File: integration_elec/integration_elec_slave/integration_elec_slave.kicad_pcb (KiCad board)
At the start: 4 copper layers, 102 parts, among them J1 CONN_02X05, J2 USB_C_Receptacle_USB2.0_16P, J3 Conn_01x03_Pin, J4 Conn_01x04_Pin, J5 Conn_01x04_Pin, Q1 Q_NMOS_GSD, Q2 Q_NMOS_GSD, Q3 Q_NMOS_GSD, SW1 SW_Push, U1 XBEE_PRO_900HP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

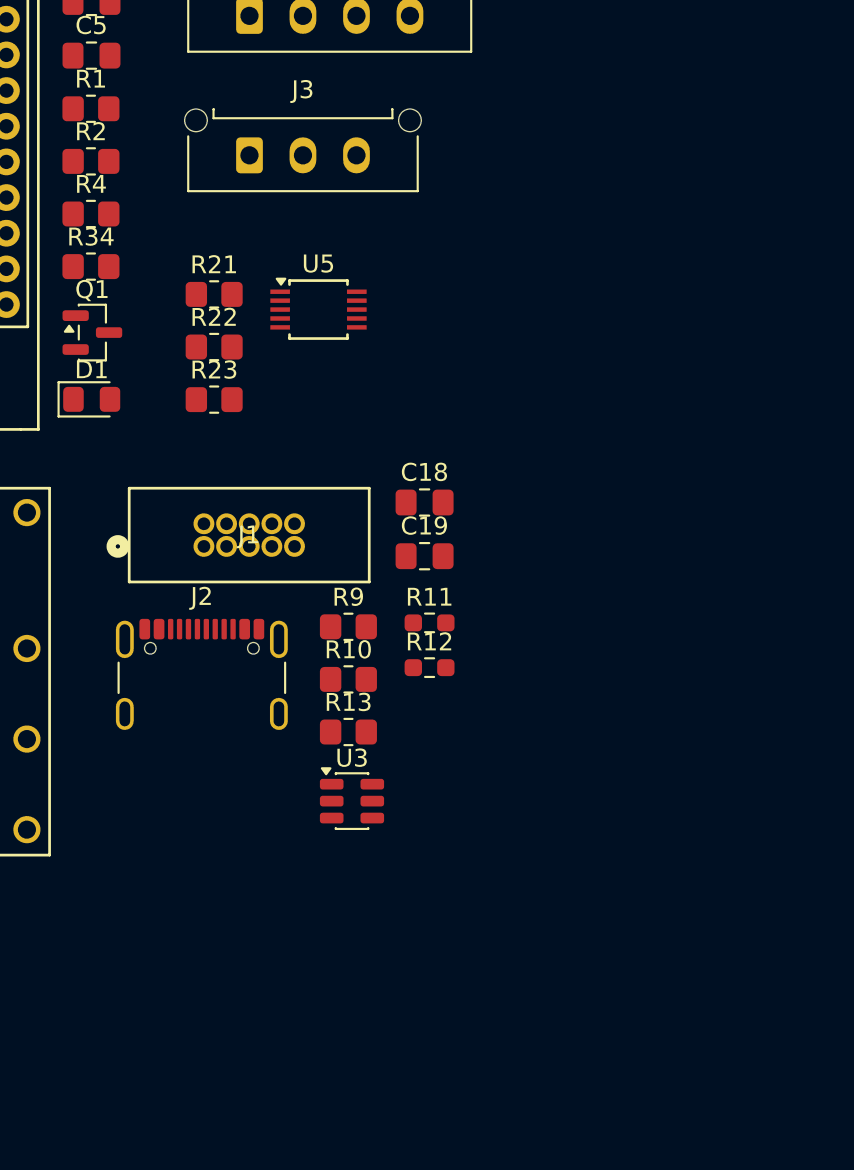
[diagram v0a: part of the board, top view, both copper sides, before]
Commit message: EM - Ajout John Pork et debut schematic
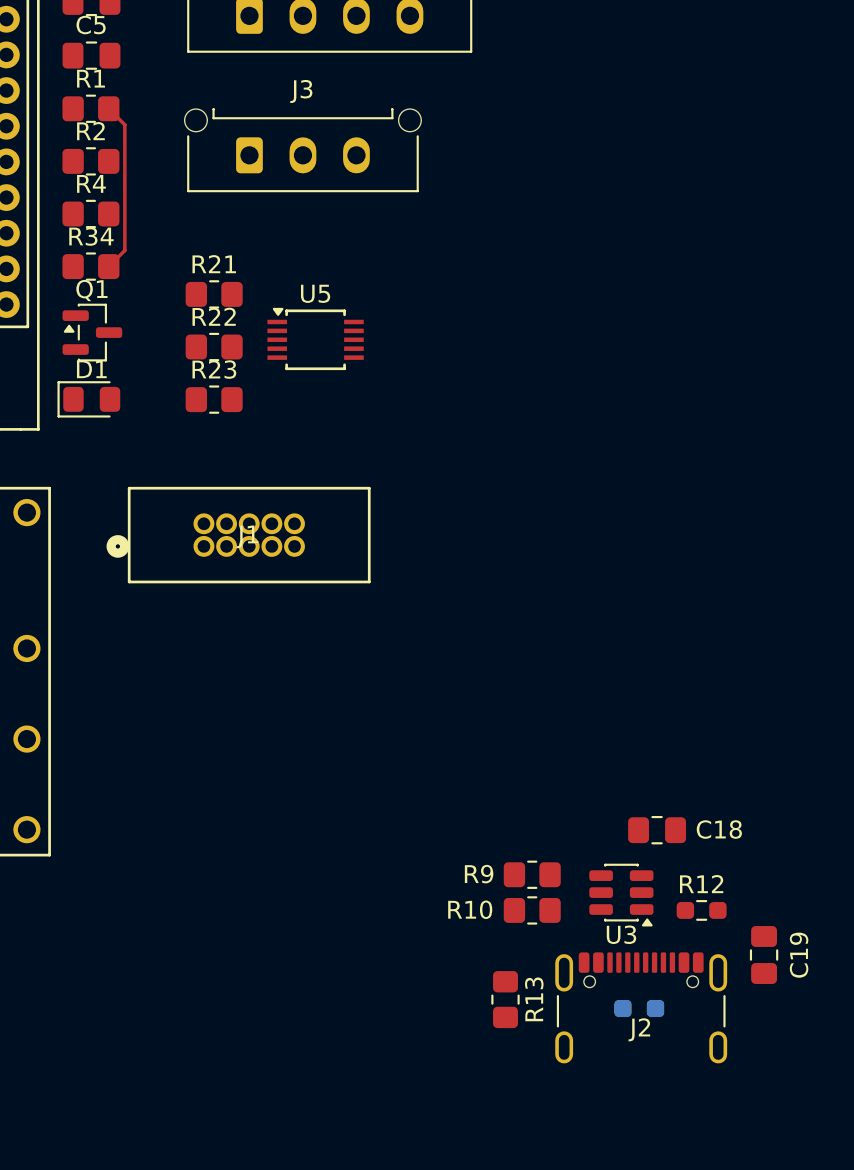
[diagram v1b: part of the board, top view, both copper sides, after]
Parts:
- R11: moved to B.Cu
- moved J2 30.9 mm to (235.1, 116.1)
- moved C19 29.4 mm to (242.0, 112.0), turned to 90 degrees
- moved R11 24.6 mm to (235.0, 115.0)
- moved C18 22.5 mm to (236.0, 105.0), turned to 180 degrees
- moved R12 20.4 mm to (238.5, 109.5)
- moved R13 17.4 mm to (227.5, 114.5), turned to -90 degrees
- moved R9 17.3 mm to (229.0, 107.5), turned to 180 degrees
- moved R10 16.6 mm to (229.0, 109.5), turned to 180 degrees
- moved U3 16.0 mm to (234.0, 108.5), turned to 180 degrees
- moved U5 1.70 mm to (216.8, 77.5)
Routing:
- net Net-(U1-nDTR): track 0.00 -> 9.60 mm
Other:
- copper layers 4 -> 2

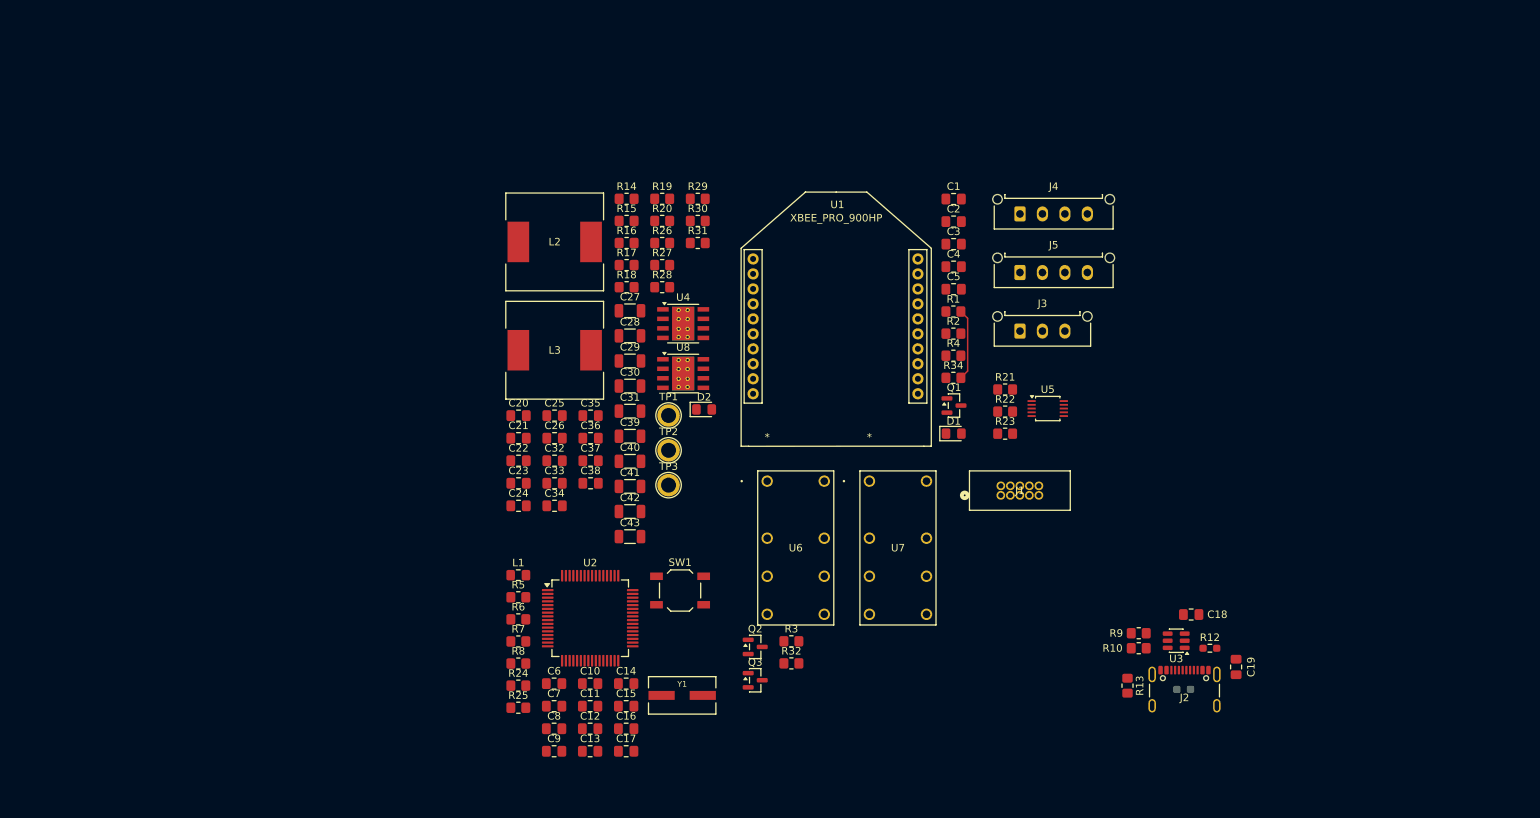
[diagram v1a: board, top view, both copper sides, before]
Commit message: EM - Fin du schématique, ajout de diode pour empêcher de backfeeder le USB. Début PCB et ajout carré 100x100
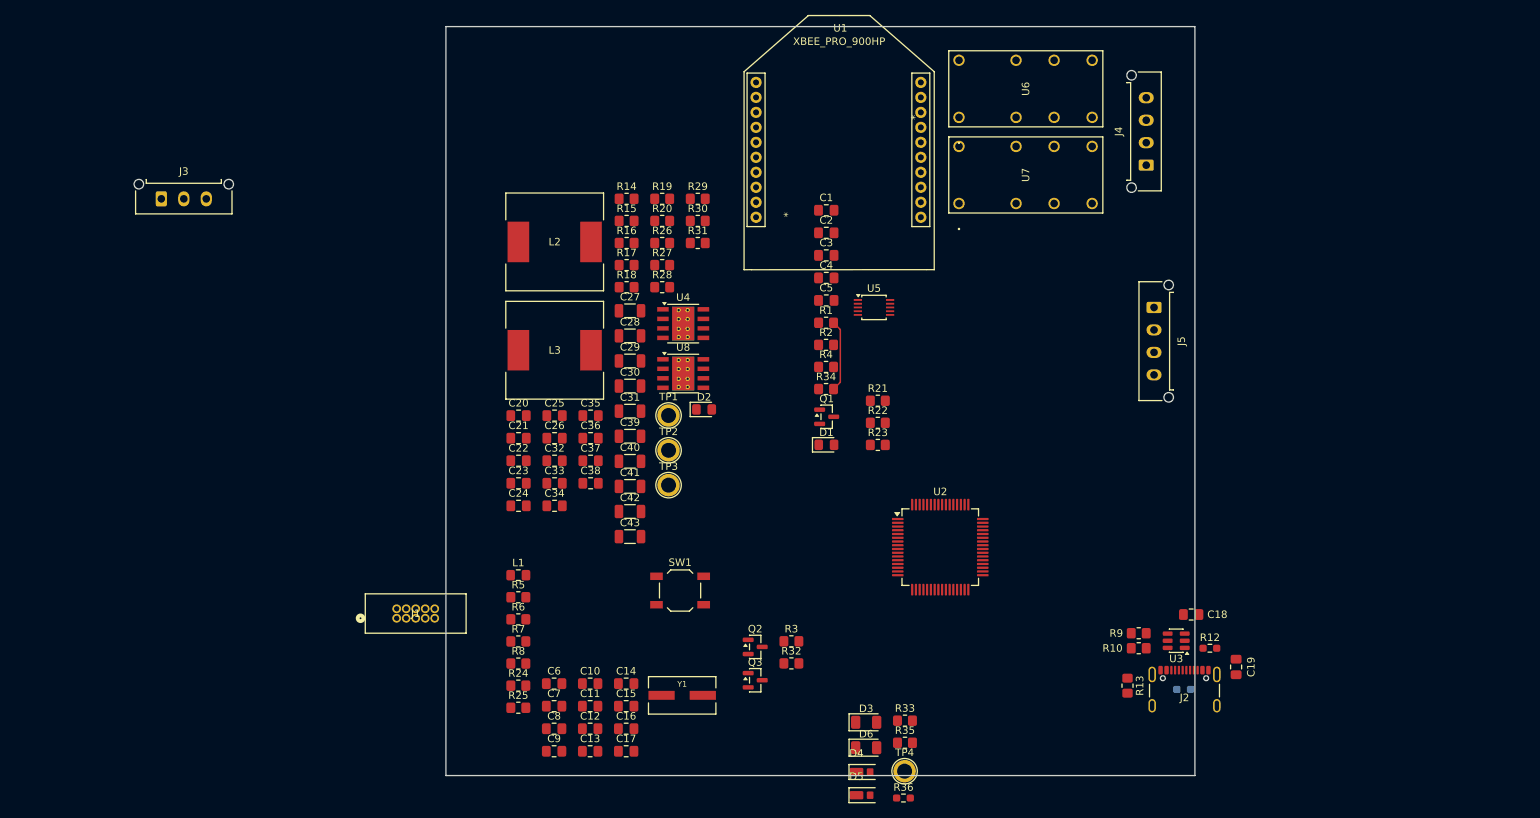
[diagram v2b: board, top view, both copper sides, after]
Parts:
- added D3: YELLOW LED, LED_SMD:LED_1206_3216Metric, F.Cu at (192.6, 119.4)
- added D4: D_Schottky, SCHTKY_DIODE:SOD323-HE, F.Cu at (191.3, 126.0)
- added D5: D_Schottky, SCHTKY_DIODE:SOD323-HE, F.Cu at (191.3, 129.1)
- added D6: GREEN LED, LED_SMD:LED_1206_3216Metric, F.Cu at (192.6, 122.8)
- added R33: 475, Resistor_SMD:R_0805_2012Metric_Pad1.20x1.40mm_HandSolder, F.Cu at (197.8, 119.2)
- added R35: 165, Resistor_SMD:R_0805_2012Metric_Pad1.20x1.40mm_HandSolder, F.Cu at (197.8, 122.1)
- added R36: 10k0, Resistor_SMD:R_0603_1608Metric_Pad0.98x0.95mm_HandSolder, F.Cu at (197.6, 129.5)
- added TP4: 12V+, TestPoint:TestPoint_Plated_Hole_D2.0mm, F.Cu at (197.7, 125.9)
- moved J3 116.0 mm to (98.5, 49.5)
- moved J1 82.3 mm to (129.9, 105.5)
- moved U6 54.9 mm to (205.0, 38.6), turned to 90 degrees
- moved U2 47.7 mm to (202.5, 96.0)
- moved U7 39.0 mm to (205.0, 50.1), turned to 90 degrees
- moved U5 26.8 mm to (193.7, 64.0)
- moved U1 23.6 mm to (177.9, 34.0)
- moved J5 18.5 mm to (231.0, 64.0), turned to -90 degrees
- moved J4 18.1 mm to (230.0, 45.0), turned to 90 degrees
- moved C1 17.1 mm to (187.3, 51.0)
- moved C2 17.1 mm to (187.3, 54.0)
- moved C3 17.1 mm to (187.3, 57.0)
- moved C4 17.1 mm to (187.3, 60.1)
- moved C5 17.1 mm to (187.3, 63.1)
- moved D1 17.1 mm to (187.3, 82.3)
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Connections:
- C20 pad 2: +12V -> /Regulator/REG_IN
- C21 pad 2: +12V -> /Regulator/REG_IN
- C22 pad 2: +12V -> /Regulator/REG_IN
- C23 pad 1: +12V -> /Regulator/REG_IN
- C32 pad 2: +12V -> /Regulator/REG_IN
- C33 pad 2: +12V -> /Regulator/REG_IN
- C34 pad 2: +12V -> /Regulator/REG_IN
- C35 pad 1: +12V -> /Regulator/REG_IN
- R14 pad 1: +12V -> /Regulator/REG_IN
- R26 pad 1: +12V -> /Regulator/REG_IN
- U4 pad 2: +12V -> /Regulator/REG_IN
- U8 pad 2: +12V -> /Regulator/REG_IN
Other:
- board outline added: 100 x 100 mm

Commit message: EM - Avancement du placement du PCB, fini USB et RELAIS, en train de continuer micro et regulateurs
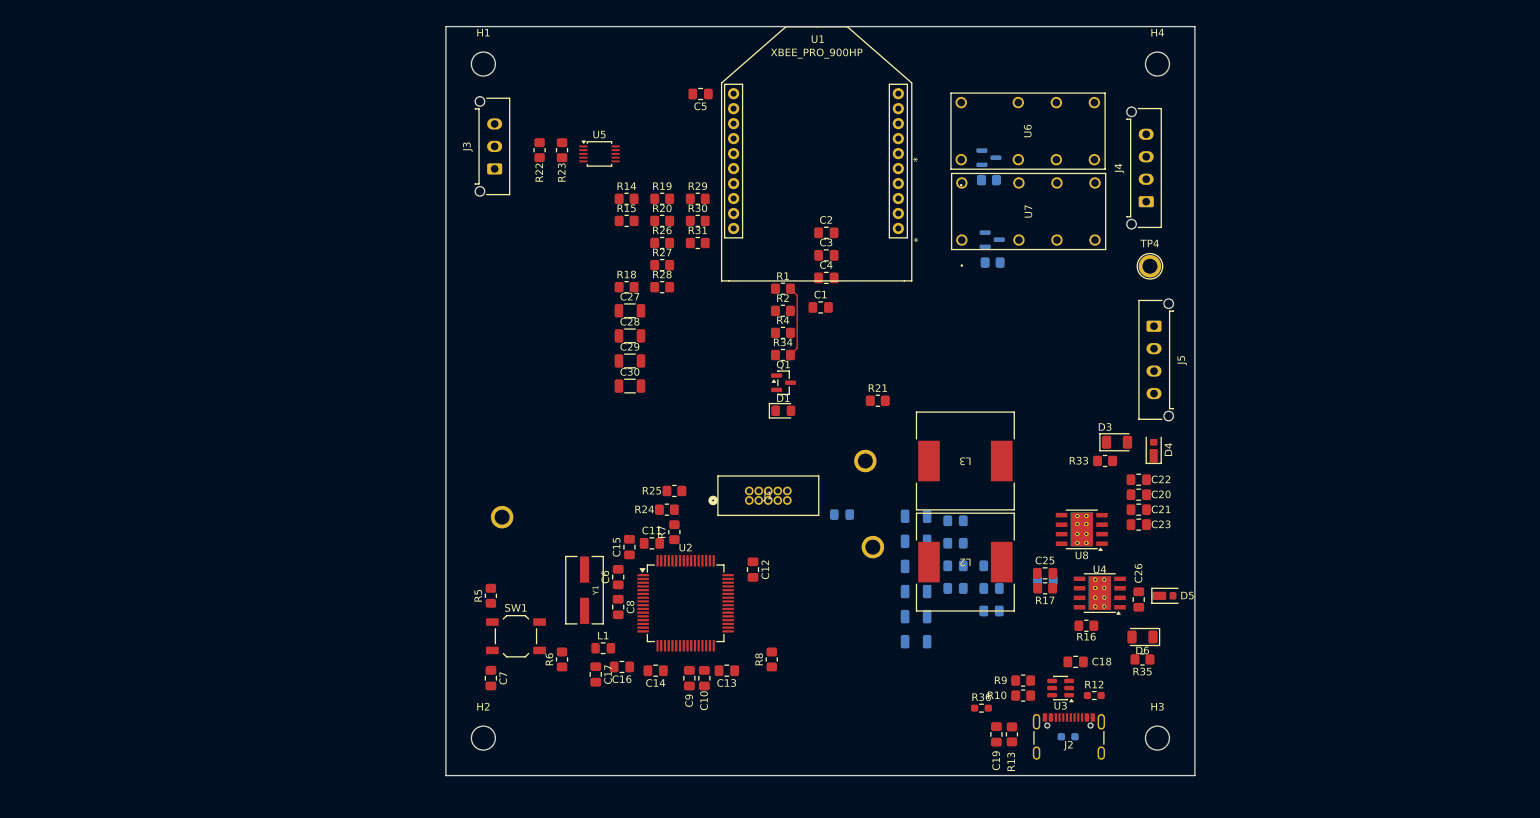
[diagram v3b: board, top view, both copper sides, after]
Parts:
- added H1: MountingHole, MountingHole:MountingHole_3.2mm_M3, F.Cu at (141.5, 31.5)
- added H2: MountingHole, MountingHole:MountingHole_3.2mm_M3, F.Cu at (141.5, 121.5)
- added H3: MountingHole, MountingHole:MountingHole_3.2mm_M3, F.Cu at (231.5, 121.5)
- added H4: MountingHole, MountingHole:MountingHole_3.2mm_M3, F.Cu at (231.5, 31.5)
- C24, C31, C32, C33, C34, C35, C36, C37, C38, C39, C40, C41, C42, C43, D2, Q2, Q3, R3, R32, TP1, TP2, TP3: moved to B.Cu
- U6, U7: footprint RELAY:RELAY8_J104D2C12VDC.20S_CRS -> RELAYS:RELAY8_J104D2C12VDC.20S_CRS
- moved C20 83.5 mm to (229.0, 89.0)
- moved C21 83.4 mm to (229.0, 91.0)
- moved C23 83.0 mm to (229.0, 93.0), turned to 180 degrees
- moved C22 82.8 mm to (229.0, 87.0)
- moved C26 80.9 mm to (229.0, 103.0), turned to 90 degrees
- moved R16 79.9 mm to (222.0, 106.5)
- moved TP4 75.0 mm to (230.5, 58.5)
- moved Q2 72.4 mm to (209.0, 44.0)
- moved C24 71.1 mm to (216.5, 100.5), turned to 180 degrees
- moved R17 70.6 mm to (216.5, 101.5), turned to 180 degrees
- moved L2 69.5 mm to (205.9, 98.0), turned to 180 degrees
- moved C25 68.8 mm to (216.5, 99.5)
- moved R3 67.0 mm to (209.0, 47.0)
- moved Q3 66.8 mm to (209.4, 55.0)
- moved U4 66.2 mm to (223.8, 102.1), turned to 180 degrees
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
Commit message: EM - Ajout du copper zone et chaise musicale pour le micro et le USB
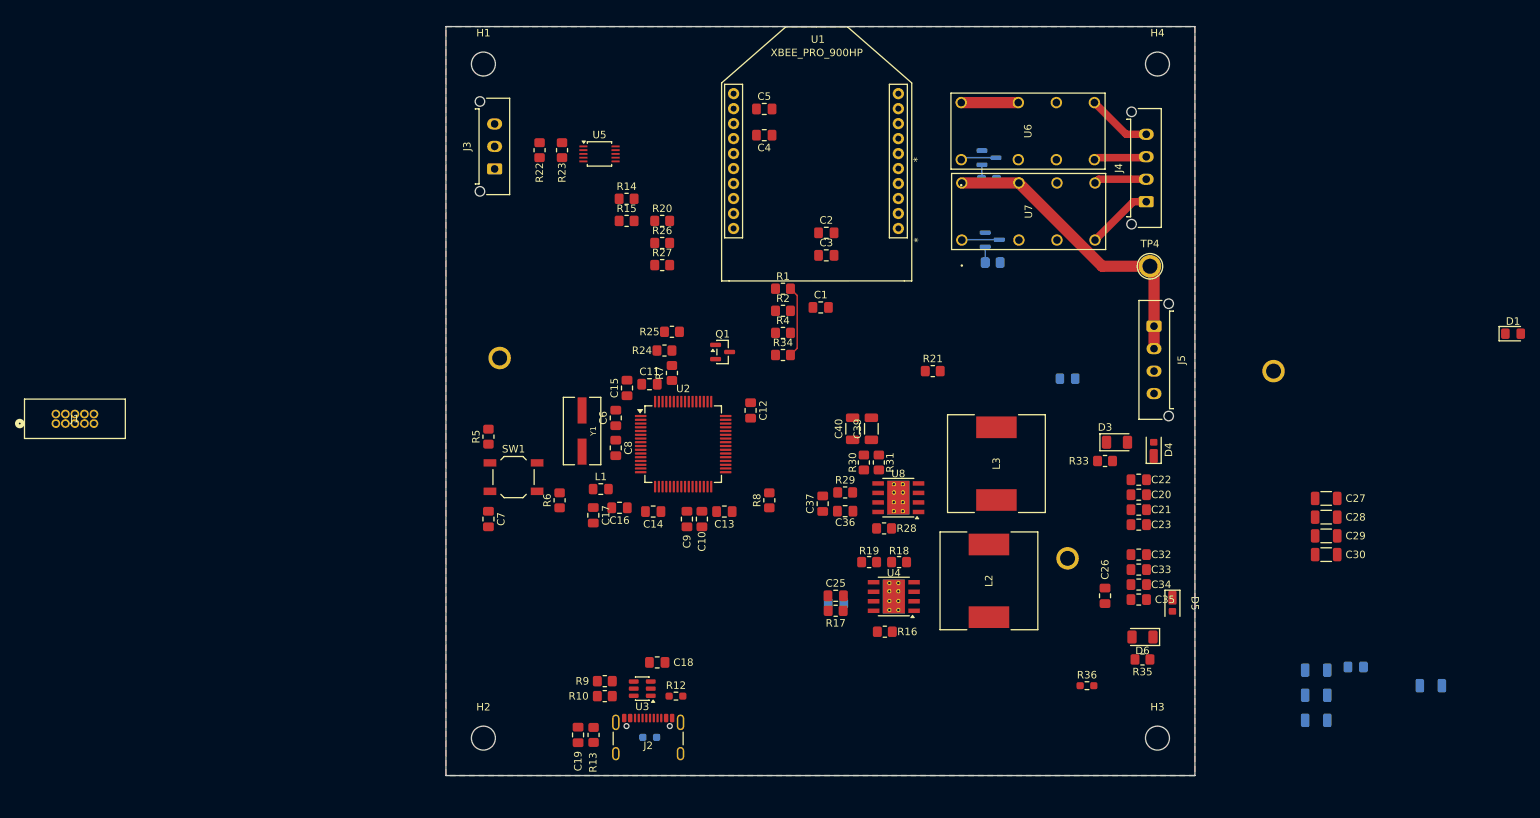
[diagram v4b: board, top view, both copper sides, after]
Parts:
- C32, C33, C34, C35, C36, C37, C39, C40: moved to F.Cu
- moved D1 98.0 mm to (279.0, 67.5)
- moved C27 96.3 mm to (254.0, 89.5)
- moved C28 96.1 mm to (254.0, 92.0)
- moved C29 95.8 mm to (254.0, 94.5)
- moved C30 95.6 mm to (254.0, 97.0)
- moved J1 93.1 mm to (84.4, 79.5)
- moved C31 72.3 mm to (268.0, 114.5)
- moved J2 56.2 mm to (163.5, 122.5)
- moved C19 55.9 mm to (154.1, 121.1)
- moved C18 55.9 mm to (164.7, 111.4)
- moved R10 55.9 mm to (157.7, 115.9)
- moved R11 55.9 mm to (163.7, 121.4)
- moved R12 55.9 mm to (167.2, 115.9)
- moved R13 55.9 mm to (156.2, 121.1)
- moved R9 55.9 mm to (157.7, 113.9)
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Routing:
- net +12V: track 0.00 -> 48.6 mm
- net /CONNECTORS/SOLENOID2_-: track 0.00 -> 8.96 mm
- net /CONNECTORS/SOLENOID1_+: track 0.00 -> 8.67 mm
- net /CONNECTORS/SOLENOID1_-: track 0.00 -> 7.08 mm
- net /CONNECTORS/SOLENOID2_+: track 0.00 -> 7.05 mm
- net Net-(Q3-D): track 0.00 -> 5.02 mm
- net Net-(Q2-D): track 0.00 -> 4.75 mm
- net /GESTION_ALIM/CTRL_SOL2: track 0.00 -> 2.10 mm
- net /GESTION_ALIM/CTRL_SOL1: track 0.00 -> 2.08 mm
- added copper zone on B.Cu, net GND
- added copper zone on F.Cu, net GND

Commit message: EM - PCB pas mal terminé, on review ça soon
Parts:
- C24, C31, C41, C42, C43, D2, TP3: moved to F.Cu
- C26: moved to B.Cu
- moved J1 96.7 mm to (181.0, 84.5), turned to -90 degrees
- moved D1 81.2 mm to (198.0, 62.0)
- moved R14 73.6 mm to (202.5, 110.0), turned to 180 degrees
- moved C31 70.7 mm to (200.5, 93.5), turned to 90 degrees
- moved R15 68.9 mm to (198.5, 110.0), turned to 180 degrees
- moved C43 67.6 mm to (201.5, 75.0), turned to 90 degrees
- moved C41 67.5 mm to (196.5, 75.0), turned to 90 degrees
- moved C42 67.4 mm to (199.0, 75.0), turned to 90 degrees
- moved C27 63.7 mm to (190.5, 93.5), turned to 90 degrees
- moved C28 61.0 mm to (193.0, 93.5), turned to 90 degrees
- moved C38 60.1 mm to (204.0, 85.5), turned to 90 degrees
- moved C29 58.5 mm to (195.5, 93.5), turned to 90 degrees
- moved C30 56.1 mm to (198.0, 93.5), turned to 90 degrees
- moved R35 52.1 mm to (178.0, 119.0), turned to -90 degrees
- moved D5 52.0 mm to (183.0, 115.0), turned to 90 degrees
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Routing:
- net +3V3: track 0.00 -> 284.7 mm, vias 0 -> 4
- net /Regulator/REG_IN: track 0.00 -> 129.7 mm
- net +5V: track 0.00 -> 90.4 mm, vias 0 -> 1
- net /MCU/RF.XBEE_LED: track 0.00 -> 61.1 mm, vias 0 -> 6
- net /GESTION_ALIM/CTRL_SOL1: track 2.08 -> 61.0 mm, vias 0 -> 1
- net /MCU/DEBUG_RESET: track 0.00 -> 57.2 mm, vias 0 -> 1
- net /GESTION_ALIM/CTRL_SOL2: track 2.10 -> 55.5 mm, vias 0 -> 1
- net /MCU/RF.XBEE_UART_OUT: track 0.00 -> 50.4 mm, vias 0 -> 1
- net /MCU/RF.XBEE_STATUS: track 0.00 -> 49.0 mm, vias 0 -> 1
- net /MCU/RF.XBEE_UART_IN: track 0.00 -> 48.0 mm, vias 0 -> 4
- net /MCU/RF.XBEE_UART_RTS: track 0.00 -> 47.7 mm, vias 0 -> 3
- net /ADC/INT_ADC_OD: track 0.00 -> 46.0 mm, vias 0 -> 2
- net /MCU/RF.XBEE_UART_CTS: track 0.00 -> 43.1 mm, vias 0 -> 1
- net /MCU/USB_D-: track 0.00 -> 41.0 mm
- net /MCU/USB_VBUS: track 0.00 -> 40.0 mm
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
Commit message: EM - Attente de review, complété avec les 3D
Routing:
- net GND: vias 8 -> 64

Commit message: EM - Oublié de run le script de via-stitching
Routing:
- net GND: vias 64 -> 905

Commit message: EM - Review pas mal finale
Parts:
- added G***: LOGO, LOGO, F.Cu at (147.0, 103.0)
- added G***: LOGO, LOGO, B.Cu at (159.3, 93.4)
- added G***: LOGO, LOGO, B.Cu at (206.9, 73.9)
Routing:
- net GND: track 25.5 -> 32.1 mm, vias 905 -> 878
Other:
- board text added: "12V"
- board text added: "3.3"
- board text added: "5V"
- board text added: "GND"
- board text added: "JTAG DEBUG"
- board text added: "POWER_IN_12V"
- board text added: "PRESSURE METER"
- board text added: "RESET SWITCH"
- board text added: "SOLENOIDS"
